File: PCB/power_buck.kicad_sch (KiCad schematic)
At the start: 6 parts

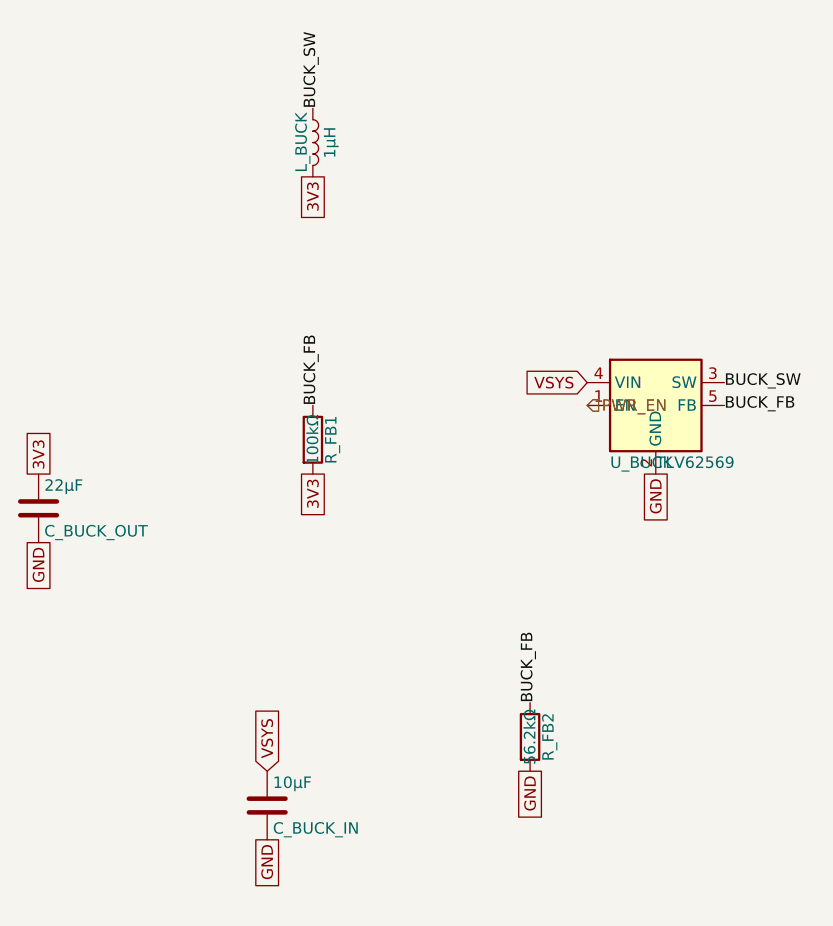
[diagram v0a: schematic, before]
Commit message: refactor: erc is clean
This gets the schematic as clean as it can be.
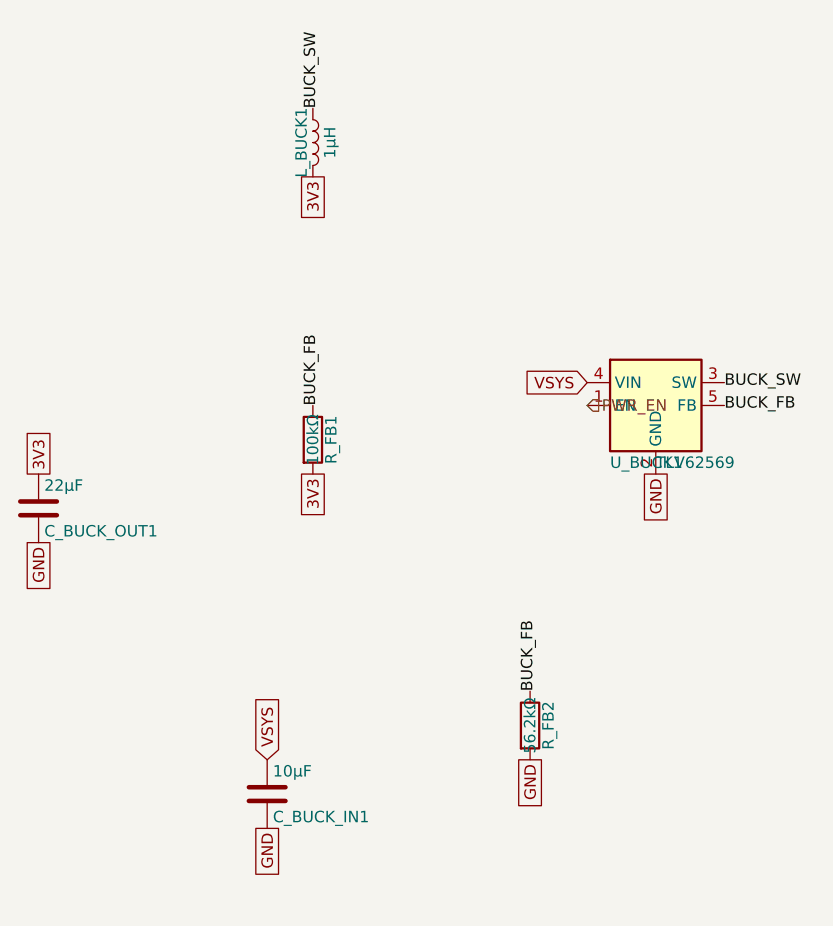
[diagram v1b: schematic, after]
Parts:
- removed C_BUCK_IN: 10µF, symbol Device:C
- removed C_BUCK_OUT: 22µF, symbol Device:C
- removed L_BUCK: 1µH, symbol Device:L
- removed U_BUCK: TLV62569, Package_TO_SOT_SMD:SOT-23-5, symbol Regulator_Switching:TLV62569DBV
- added C_BUCK_IN1: 10µF, symbol Device:C
- added C_BUCK_OUT1: 22µF, symbol Device:C
- added L_BUCK1: 1µH, symbol Device:L
- added U_BUCK1: TLV62569, Package_TO_SOT_SMD:SOT-23-5, symbol Regulator_Switching:TLV62569DBV
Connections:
- net 3V3: now also C_BUCK_OUT1.1, L_BUCK1.2
- net BUCK_FB: now also U_BUCK1.5 (FB)
- net BUCK_SW: now also L_BUCK1.1, U_BUCK1.3 (SW)
- net GND: now also C_BUCK_IN1.2, C_BUCK_OUT1.2, U_BUCK1.2 (GND)
- net PWR_EN: now also U_BUCK1.1 (EN)
- net VSYS: now also C_BUCK_IN1.1, U_BUCK1.4 (VIN)

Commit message: refactor: switch over to esp32-s3-wroom1 (#13)
This refactors to the esp32-s3 to avoid every problem we encountered with the raspberry pi options.
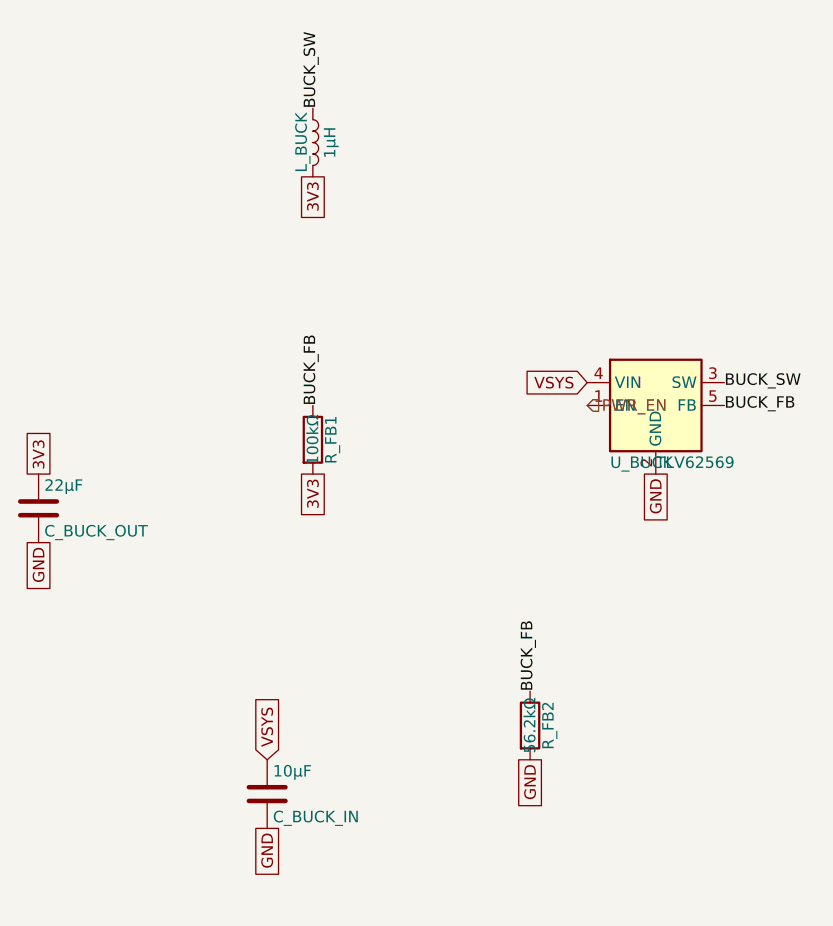
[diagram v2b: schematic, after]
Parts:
- removed C_BUCK_IN1: 10µF, symbol Device:C
- removed C_BUCK_OUT1: 22µF, symbol Device:C
- removed L_BUCK1: 1µH, symbol Device:L
- removed U_BUCK1: TLV62569, Package_TO_SOT_SMD:SOT-23-5, symbol Regulator_Switching:TLV62569DBV
- added C_BUCK_IN: 10µF, Capacitor_SMD:C_0805_2012Metric, symbol Device:C
- added C_BUCK_OUT: 22µF, Capacitor_SMD:C_0805_2012Metric, symbol Device:C
- added L_BUCK: 1µH, Inductor_SMD:L_Bourns_SRR1260, symbol Device:L
- added U_BUCK: TLV62569, Package_TO_SOT_SMD:SOT-23-5, symbol Regulator_Switching:TLV62569DBV
- R_FB1, R_FB2: footprint (none) -> Resistor_SMD:R_0402_1005Metric
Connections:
- net 3V3: now also C_BUCK_OUT.1, L_BUCK.2
- net BUCK_FB: now also U_BUCK.5 (FB)
- net BUCK_SW: now also L_BUCK.1, U_BUCK.3 (SW)
- net GND: now also C_BUCK_IN.2, C_BUCK_OUT.2, U_BUCK.2 (GND)
- net PWR_EN: now also U_BUCK.1 (EN)
- net VSYS: now also C_BUCK_IN.1, U_BUCK.4 (VIN)

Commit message: cleanup: annotations and library updates
This is just a task to update the kicad libraries and annotations internally to get that clean ERC.
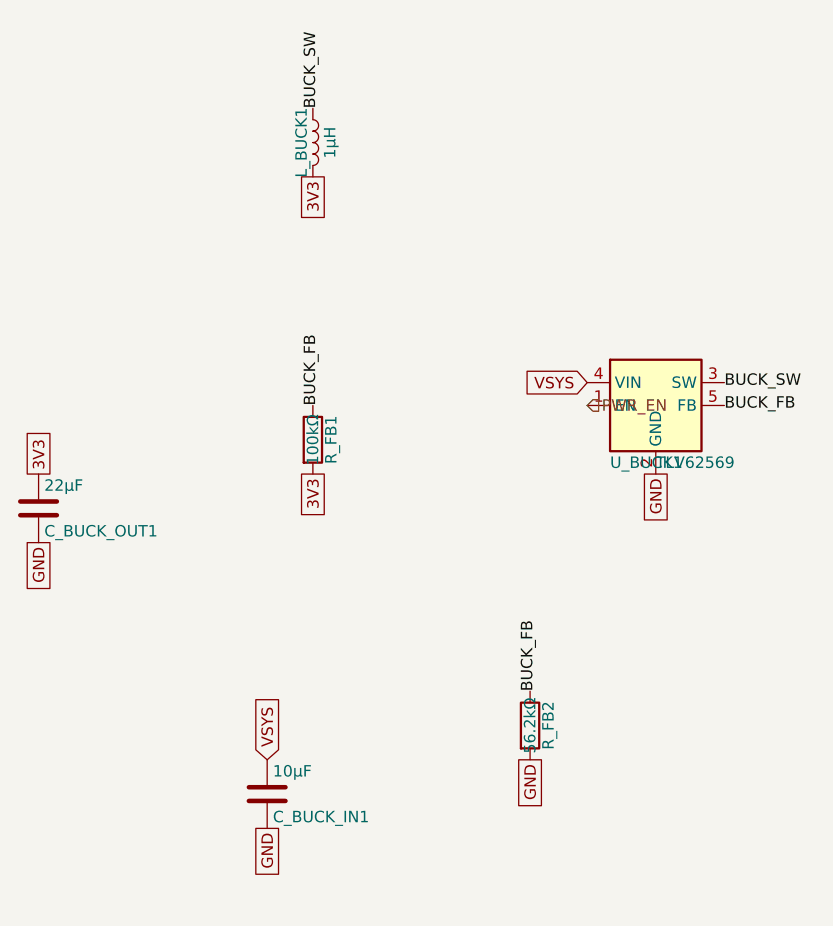
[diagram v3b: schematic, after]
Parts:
- renumbered C_BUCK_IN to C_BUCK_IN1, C_BUCK_OUT to C_BUCK_OUT1, L_BUCK to L_BUCK1, U_BUCK to U_BUCK1
